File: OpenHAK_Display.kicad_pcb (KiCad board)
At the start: 2 copper layers, 21 x 21.6 mm, 10 parts, among them P1 CONN_01X08

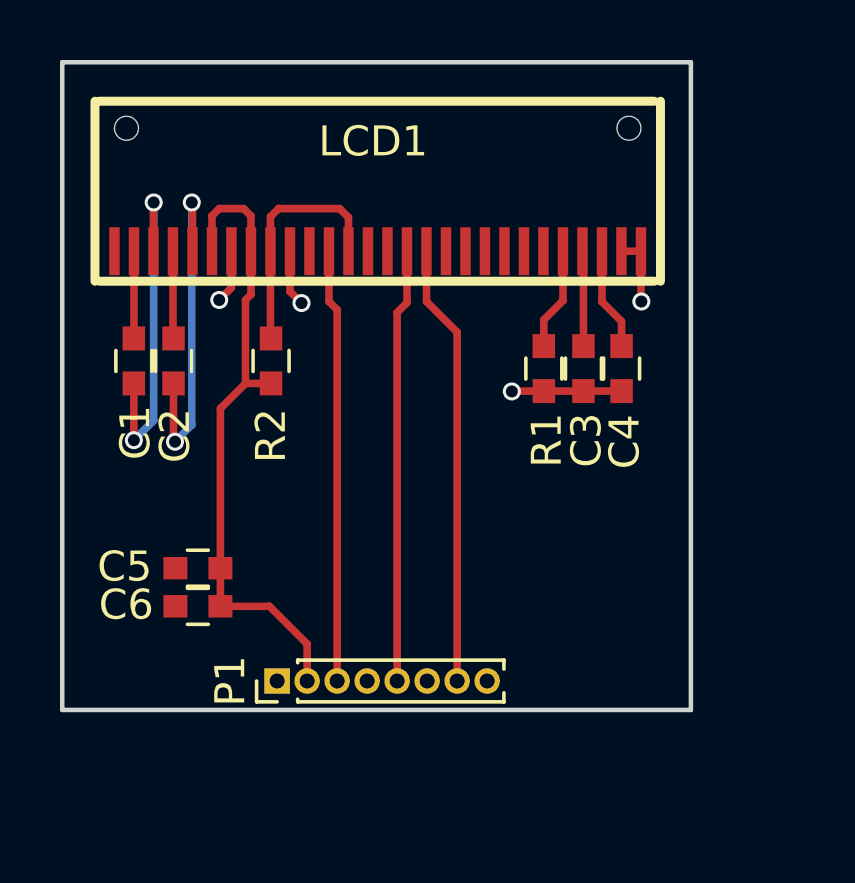
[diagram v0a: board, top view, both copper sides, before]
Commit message: redesign layout for new hardware
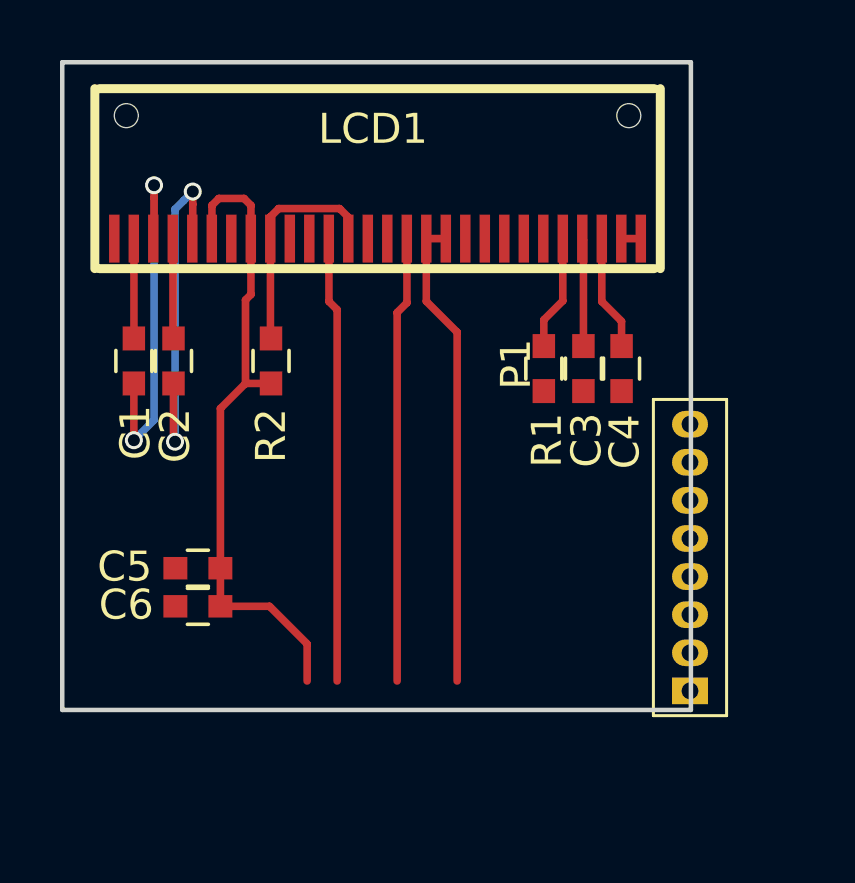
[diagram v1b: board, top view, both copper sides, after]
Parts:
- P1: footprint Pin_Headers:Pin_Header_Straight_1x08_Pitch1.00mm -> Solutions:8_pin_Castellation_127
- moved P1 14.4 mm to (137.1, 104.5)
- moved LCD1 0.42 mm to (126.7, 93.9)
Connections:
- LCD1 pad 18: Net-(LCD1-Pad18) -> /SDA
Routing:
- net GND: track 9.68 -> 0.65 mm, vias 4 -> 0
- net Net-(C1-Pad2): track 11.7 -> 12.9 mm
- net /SDA: track 14.7 -> 15.8 mm
- net Net-(C3-Pad2): track 3.18 -> 4.02 mm
- net Net-(C2-Pad2): track 11.8 -> 12.5 mm
- net +3V3: track 21.6 -> 22.3 mm
- added copper zone on B.Cu, net +3V3
- removed copper zone on F.Cu, net GND
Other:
- rule pad_to_mask_clearance: 0.2 -> 0.05

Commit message: swapped 0603 for 0402
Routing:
- net +3V3: track 22.3 -> 0.00 mm
- net /SDA: track 15.8 -> 0.65 mm
- net /SCL: track 14.5 -> 0.00 mm
- net /OLED_RST: track 14.4 -> 0.00 mm
- net Net-(C1-Pad2): track 12.9 -> 0.03 mm, vias 2 -> 0
- net Net-(C2-Pad2): track 12.5 -> 0.01 mm, vias 2 -> 0
- net Net-(LCD1-Pad13): track 8.03 -> 0.00 mm
- net Net-(C4-Pad1): track 3.85 -> 0.00 mm
- net Net-(LCD1-Pad24): track 3.84 -> 0.00 mm
- net Net-(C3-Pad2): track 4.02 -> 0.42 mm
- net Net-(C2-Pad1): track 2.91 -> 0.00 mm
- net Net-(C1-Pad1): track 2.91 -> 0.00 mm
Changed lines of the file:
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@@
     (thickness 1.6)
     (drawings 19)
-    (tracks 65)
+    (tracks 6)
     (zones 0)
     (modules 10)
@@
   )
   (setup
-    (last_trace_width 0.254)
+    (last_trace_width 0.25)
     (user_trace_width 0.2032)
     (user_trace_width 0.254)
@@
   (module Solutions:8_pin_Castellation_127 (layer F.Cu)
     (at 137.13 104.521 90)
-    (fp_text reference P1 (at 6.445 -5.8 90) (layer F.SilkS)
+    (fp_text reference P1 (at -4.04 -1.945 90) (layer F.SilkS)
       (effects (font (size 1 1) (thickness 0.15)))
     )
@@
     (arrow2b (pts (xy 136.144 85.344) (xy 137.270504 84.757579)))
   )
-  (segment (start 118.5926 98.7178) (end 118.5926 100.6094) (width 0.254) (layer F.Cu) (net 1))
-  (via (at 118.5926 100.6094) (size 0.6) (drill 0.4) (layers F.Cu B.Cu) (net 1))
-  (via (at 119.265 92.111) (size 0.6) (drill 0.4) (layers F.Cu B.Cu) (net 1))
   (segment (start 119.2456 94.3102) (end 119.265 94.2908) (width 0.254) (layer F.Cu) (net 1))
-  (segment (start 119.265 94.2908) (end 119.265 92.535264) (width 0.254) (layer F.Cu) (net 1))
-  (segment (start 118.5926 100.6094) (end 119.265 99.937) (width 0.254) (layer B.Cu) (net 1))
-  (segment (start 119.265 92.535264) (end 119.265 92.111) (width 0.254) (layer F.Cu) (net 1))
-  (segment (start 119.265 99.937) (end 119.265 92.535264) (width 0.254) (layer B.Cu) (net 1))
-  (segment (start 119.265 92.535264) (end 119.265 92.111) (width 0.254) (layer B.Cu) (net 1))
-  (segment (start 118.5956 94.3102) (end 118.5956 97.2148) (width 0.254) (layer F.Cu) (net 2))
-  (segment (start 118.5956 97.2148) (end 118.5926 97.2178) (width 0.254) (layer F.Cu) (net 2))
-  (segment (start 119.9134 98.7178) (end 119.9134 100.6094) (width 0.254) (layer F.Cu) (net 3))
-  (via (at 119.9642 100.6602) (size 0.6) (drill 0.4) (layers F.Cu B.Cu) (net 3))
-  (segment (start 119.9134 100.6094) (end 119.9642 100.6602) (width 0.254) (layer F.Cu) (net 3))
-  (via (at 120.555 92.321) (size 0.6) (drill 0.4) (layers F.Cu B.Cu) (net 3))
   (segment (start 120.5456 94.3102) (end 120.555 94.3008) (width 0.254) (layer F.Cu) (net 3))
-  (segment (start 120.555 92.745264) (end 120.555 92.321) (width 0.254) (layer F.Cu) (net 3))
-  (segment (start 119.9642 100.6602) (end 119.9642 92.9118) (width 0.254) (layer B.Cu) (net 3))
-  (segment (start 119.9642 92.9118) (end 120.255001 92.620999) (width 0.254) (layer B.Cu) (net 3))
-  (segment (start 120.555 94.3008) (end 120.555 92.745264) (width 0.254) (layer F.Cu) (net 3))
-  (segment (start 120.255001 92.620999) (end 120.555 92.321) (width 0.254) (layer B.Cu) (net 3))
-  (segment (start 119.8956 94.3102) (end 119.8956 97.2) (width 0.254) (layer F.Cu) (net 4))
-  (segment (start 119.8956 97.2) (end 119.9134 97.2178) (width 0.254) (layer F.Cu) (net 4))
   (segment (start 133.54 94.3046) (end 133.5456 94.3102) (width 0.254) (layer F.Cu) (net 5))
   (segment (start 133.54 93.891) (end 133.54 94.3046) (width 0.254) (layer F.Cu) (net 5))
-  (segment (start 133.5786 93.9296) (end 133.54 93.891) (width 0.254) (layer F.Cu) (net 5))
-  (segment (start 133.5786 97.4718) (end 133.5786 93.9296) (width 0.254) (layer F.Cu) (net 5))
   (segment (start 135.49 93.891) (end 134.84 93.891) (width 0.254) (layer F.Cu) (net 6))
-  (segment (start 134.19 95.9884) (end 134.19 93.891) (width 0.254) (layer F.Cu) (net 7))
-  (segment (start 134.8486 96.647) (end 134.19 95.9884) (width 0.254) (layer F.Cu) (net 7))
-  (segment (start 134.8486 97.4718) (end 134.8486 96.647) (width 0.254) (layer F.Cu) (net 7))
-  (segment (start 121.4762 104.8766) (end 121.4762 99.5546) (width 0.254) (layer F.Cu) (net 8))
-  (segment (start 122.313 98.7178) (end 123.1646 98.7178) (width 0.254) (layer F.Cu) (net 8))
-  (segment (start 121.4762 99.5546) (end 122.313 98.7178) (width 0.254) (layer F.Cu) (net 8))
-  (segment (start 124.3678 108.6358) (end 124.3678 107.4006) (width 0.254) (layer F.Cu) (net 8))
-  (segment (start 123.1138 106.1466) (end 121.4762 106.1466) (width 0.254) (layer F.Cu) (net 8))
-  (segment (start 124.3678 107.4006) (end 123.1138 106.1466) (width 0.254) (layer F.Cu) (net 8))
-  (segment (start 121.4762 104.8766) (end 121.4762 106.1466) (width 0.254) (layer F.Cu) (net 8))
-  (segment (start 122.4956 95.7532) (end 122.313 95.9358) (width 0.254) (layer F.Cu) (net 8))
-  (segment (start 121.1956 92.7804) (end 121.425 92.551) (width 0.254) (layer F.Cu) (net 8))
-  (segment (start 122.265 92.551) (end 122.4956 92.7816) (width 0.254) (layer F.Cu) (net 8))
-  (segment (start 122.313 95.9358) (end 122.313 98.7178) (width 0.254) (layer F.Cu) (net 8))
-  (segment (start 121.425 92.551) (end 122.265 92.551) (width 0.254) (layer F.Cu) (net 8))
-  (segment (start 122.4956 92.7816) (end 122.4956 95.7532) (width 0.254) (layer F.Cu) (net 8))
-  (segment (start 121.1956 94.3102) (end 121.1956 92.7804) (width 0.254) (layer F.Cu) (net 8))
-  (segment (start 123.1456 94.3102) (end 123.1456 93.1608) (width 0.254) (layer F.Cu) (net 9))
-  (segment (start 125.7456 93.1828) (end 125.7456 94.3102) (width 0.254) (layer F.Cu) (net 9))
-  (segment (start 125.4506 92.8878) (end 125.7456 93.1828) (width 0.254) (layer F.Cu) (net 9))
-  (segment (start 123.4186 92.8878) (end 125.4506 92.8878) (width 0.254) (layer F.Cu) (net 9))
-  (segment (start 123.1456 93.1608) (end 123.4186 92.8878) (width 0.254) (layer F.Cu) (net 9))
-  (segment (start 123.1456 94.3102) (end 123.1456 97.1988) (width 0.254) (layer F.Cu) (net 9))
-  (segment (start 123.1456 97.1988) (end 123.1646 97.2178) (width 0.254) (layer F.Cu) (net 9))
-  (segment (start 125.3678 108.6358) (end 125.3678 96.2594) (width 0.254) (layer F.Cu) (net 11))
-  (segment (start 125.0956 95.9872) (end 125.0956 94.3102) (width 0.254) (layer F.Cu) (net 11))
-  (segment (start 125.3678 96.2594) (end 125.0956 95.9872) (width 0.254) (layer F.Cu) (net 11))
-  (segment (start 127.3678 108.6358) (end 127.3678 96.3554) (width 0.254) (layer F.Cu) (net 14))
-  (segment (start 127.6956 96.0276) (end 127.6956 94.3102) (width 0.254) (layer F.Cu) (net 14))
-  (segment (start 127.3678 96.3554) (end 127.6956 96.0276) (width 0.254) (layer F.Cu) (net 14))
-  (segment (start 128.34 95.9804) (end 128.34 93.891) (width 0.254) (layer F.Cu) (net 15))
-  (segment (start 129.3678 97.0082) (end 128.34 95.9804) (width 0.254) (layer F.Cu) (net 15))
-  (segment (start 129.3678 108.6358) (end 129.3678 97.0082) (width 0.254) (layer F.Cu) (net 15))
   (segment (start 128.34 93.891) (end 128.99 93.891) (width 0.254) (layer F.Cu) (net 15))
-  (segment (start 132.89 95.964) (end 132.89 93.891) (width 0.254) (layer F.Cu) (net 21))
-  (segment (start 132.2578 96.5962) (end 132.89 95.964) (width 0.254) (layer F.Cu) (net 21))
-  (segment (start 132.2578 97.4718) (end 132.2578 96.5962) (width 0.254) (layer F.Cu) (net 21))
   (zone (net 8) (net_name +3V3) (layer B.Cu) (hatch edge 0.508)
     (connect_pads (clearance 0.254))

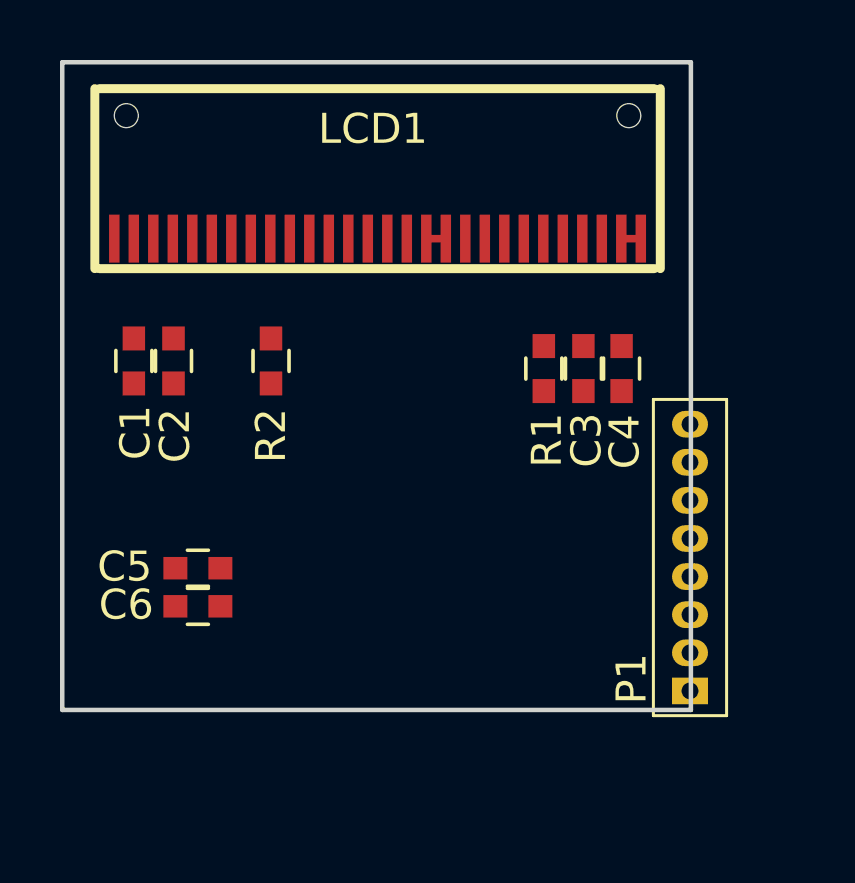
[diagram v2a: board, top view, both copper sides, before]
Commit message: repackaged library
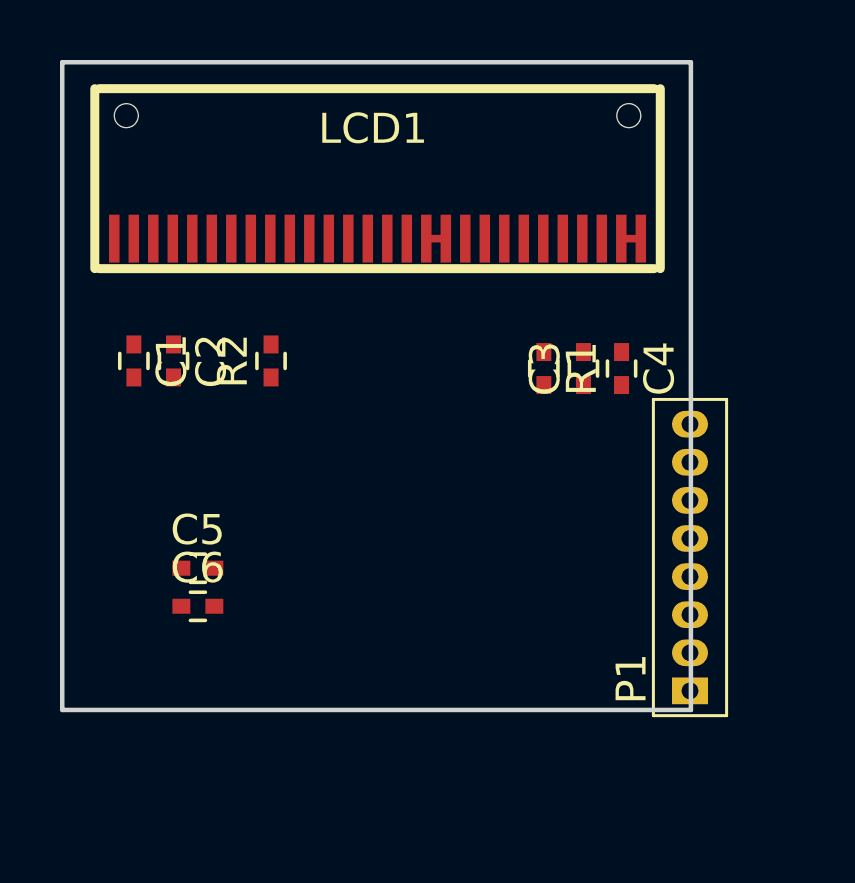
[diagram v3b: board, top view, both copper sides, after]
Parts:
- C1, C2, C3, C4, C5, C6, R1, R2: footprint Capacitors_SMD:C_0603 -> Capacitors_SMD:C_0402

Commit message: Adjusting to fit the new 10 pin breakout
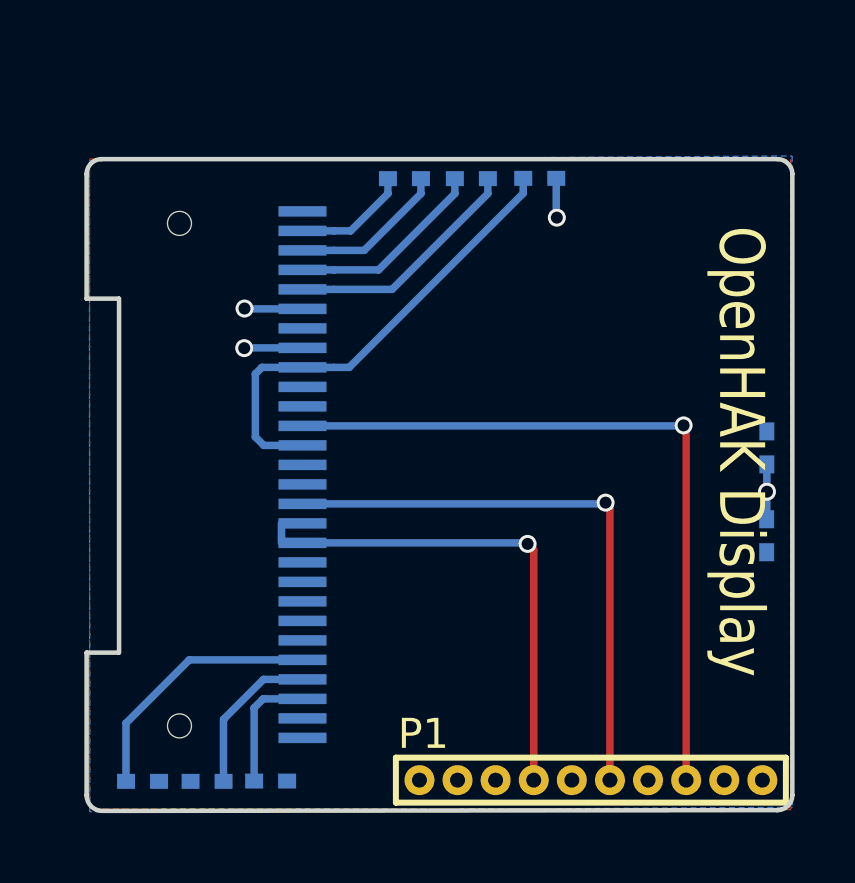
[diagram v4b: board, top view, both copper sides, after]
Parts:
- added G***: LOGO, Solutions:OHAKtemplate, F.Cu at (129.0, 101.8)
- C1, C2, C3, C4, C5, C6, LCD1, R1, R2: moved to B.Cu
- P1: value CONN_01X08 -> M52-Series_Male_TH_Harwin; footprint Solutions:8_pin_Castellation_127 -> Solutions:M52-Series_M_TH_0.05_Harwin
- moved C5 19.4 mm to (139.7, 100.9), turned to 90 degrees
- moved R1 19.2 mm to (118.9, 112.0), turned to 0 degrees
- moved C6 19.1 mm to (139.7, 103.8), turned to 270 degrees
- moved C3 18.6 mm to (121.0, 112.0), turned to 0 degrees
- moved C4 18.1 mm to (123.2, 112.0), turned to 0 degrees
- moved C2 11.6 mm to (129.8, 91.9), turned to 0 degrees
- moved C1 10.9 mm to (127.6, 91.9), turned to 0 degrees
- moved R2 10.8 mm to (132.1, 91.9), turned to 180 degrees
- moved LCD1 8.25 mm to (124.2, 101.8), turned to 270 degrees
- moved P1 8.12 mm to (133.8, 111.9), turned to 0 degrees
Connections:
- C5 pad 1: GND -> +3V3
- C5 pad 2: +3V3 -> GND
- C6 pad 1: GND -> +3V3
- C6 pad 2: +3V3 -> GND
- P1 pad 3: /OLED_RST -> Net-(P1-Pad3)
- P1 pad 4: Net-(P1-Pad4) -> /SDA
- P1 pad 5: /SCL -> Net-(P1-Pad5)
- P1 pad 6: Net-(P1-Pad6) -> /SCL
- P1 pad 7: /SDA -> Net-(P1-Pad7)
- P1 pad 8: Net-(P1-Pad8) -> /OLED_RST
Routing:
- net /OLED_RST: track 0.00 -> 24.6 mm, vias 0 -> 1
- net /SCL: track 0.00 -> 19.4 mm, vias 0 -> 1
- net Net-(LCD1-Pad13): track 0.00 -> 15.7 mm
- net /SDA: track 0.65 -> 16.1 mm, vias 0 -> 1
- net Net-(LCD1-Pad24): track 0.00 -> 8.69 mm
- net Net-(C2-Pad2): track 0.01 -> 8.01 mm
- net +3V3: track 0.00 -> 7.04 mm, vias 0 -> 4
- net Net-(C2-Pad1): track 0.00 -> 6.63 mm
- net Net-(C3-Pad2): track 0.42 -> 5.67 mm
- net Net-(C1-Pad2): track 0.03 -> 5.26 mm
- net Net-(C4-Pad1): track 0.00 -> 4.18 mm
- net Net-(C1-Pad1): track 0.00 -> 3.86 mm
- net GND: track 0.65 -> 0.00 mm
- added copper zone on F.Cu, net +3V3
- removed copper zone on B.Cu, net +3V3
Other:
- board size 21 x 21.6 mm -> 23.5 x 21.7 mm
- board text added: "21 24 OLED_RST SCL SDA 3V GND"
- board text added: "OpenHAK Dislpaly"
- board text added: "OpenHAK Display"
- board text added: "openhak.comn"

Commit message: cleaned up silk and made production files
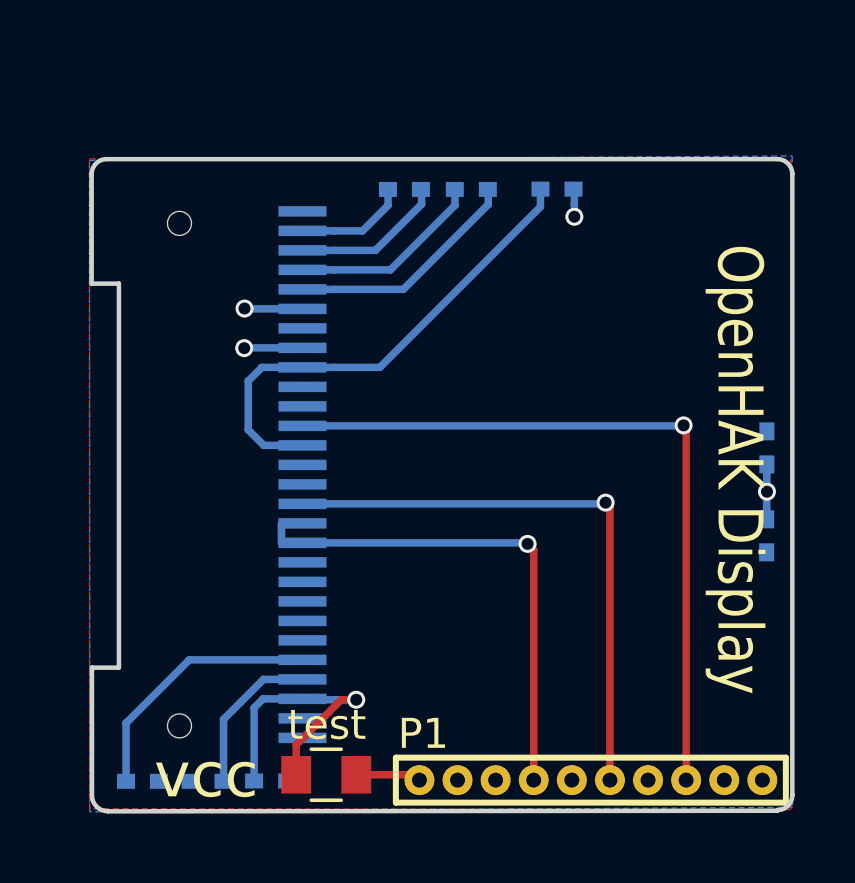
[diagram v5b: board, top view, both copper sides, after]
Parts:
- added REF***: OSHW-Logo_5.7x6mm_SilkScreen, Symbols:OSHW-Logo_5.7x6mm_SilkScreen, B.Cu at (132.8, 104.7)
- added test: TEST POINT, Capacitors_SMD:C_0805, F.Cu at (125.0, 111.8)
- moved R2 0.68 mm to (132.7, 92.2)
- moved C2 0.36 mm to (129.8, 92.3)
- moved C1 0.36 mm to (127.6, 92.3)
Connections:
- net Net-(C4-Pad1) renamed /VCC
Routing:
- net /VCC: track 4.18 -> 9.60 mm, vias 0 -> 1
- net GND: track 0.00 -> 2.18 mm
- net Net-(LCD1-Pad13): track 15.7 -> 16.4 mm
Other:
- board size 23.5 x 21.7 mm -> 23.4 x 21.7 mm
- board text added: "OLED_RST SCL SDA 3V GND"
- board text added: "vcc"
- board text removed: "21 24 OLED_RST SCL SDA 3V GND"
